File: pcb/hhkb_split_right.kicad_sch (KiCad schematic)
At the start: 73 parts, among them SW1 keyswitch, SW10 keyswitch, SW11 keyswitch, SW12 keyswitch, SW13 keyswitch, SW14 keyswitch, SW15 keyswitch, SW16 keyswitch, SW17 keyswitch, SW18 keyswitch, SW19 keyswitch, SW2 keyswitch, SW20 keyswitch, SW21 keyswitch, SW22 keyswitch, SW23 keyswitch, SW24 keyswitch, SW25 keyswitch, SW26 keyswitch, SW27 keyswitch, SW28 keyswitch, SW29 keyswitch, SW3 keyswitch, SW30 keyswitch, SW31 keyswitch, SW32 keyswitch, SW33 keyswitch, SW34 keyswitch, SW4 keyswitch, SW5 keyswitch, SW6 keyswitch, SW7 keyswitch, SW8 keyswitch, SW9 keyswitch, U1 74LVC595, U2 74LVC595

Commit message: #49 をビア/窓の露出方式で決着——部品も配線も足さず既存の銅のレジストを剥がす
利用者の提案（テストパッドは取り消し済み）。finalize_pcb.expose_debug_copper が
本番の板を作るたびに、ネットごとに他ネットの銅から最も離れた 1 点を選び:
- ビアがあれば裏面（部品面）のテンティングを外す（右: SPI_SCK/SPI_MOSI/CS/
  U1_U2/V3V3 + GND）
- ビアが無ければ配線に沿った B.Mask の窓 2.5×0.5 を開ける（左: SPI 系 4 本。
  左の SPI は全部 B.Cu だけで引かれていてビアが無い）+ GND ビア
窓幅 0.8 は隣の銅とのレジスト残りが規定を割り DRC 8 件 → 0.5 で解消。
定数は pcb_rules.py（検査環境に pcbnew が無いため）。
検査 test_every_debug_net_has_exposed_copper を追加（故意に戻して赤を確認）。
3 基板とも DRC 0/0。半田付けは AWG30 級・細いこて前提（open-gaps #49 に注記）。

Co-Authored-By: Claude Fable 5 <noreply@anthropic.com>
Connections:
- net COL0: now also SW18.1, SW25.1, SW32.1
- net COL1: now also SW17.1, SW31.1; no longer SW18.1, SW25.1, SW32.1
- net COL8: no longer SW17.1, SW31.1
- net CS: now also J_DB.4; no longer J_DB.1
- net GND: now also J_DB.1; no longer J_DB.12, J_DB.5
- net SPI_MOSI: now also J_DB.3; no longer J_DB.4
- net SPI_SCK: now also J_DB.5; no longer J_DB.3
- net SPARE2: now reaches J_DB.6
- net ROW0 renamed ROW_C
- net ROW_C: now also J_DB.10; no longer J_DB.7
- net ROW1 renamed ROW_A
- net ROW2 renamed ROW_B
- net ROW_B: now also J_DB.9; no longer J_DB.11
- net ROW3 renamed ROW_D
- net ROW_D: now also J_DB.11; no longer J_DB.10
- net ROW4 renamed ROW_E
- net ROW_E: now also J_DB.12; no longer J_DB.9
- new net SPARE: J_DB.7
- no-connect marks 9 -> 8
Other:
- moved on the sheet: D1, D10, D11, D12, D13, D14, D15, D16, D17, D18, D19, D2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

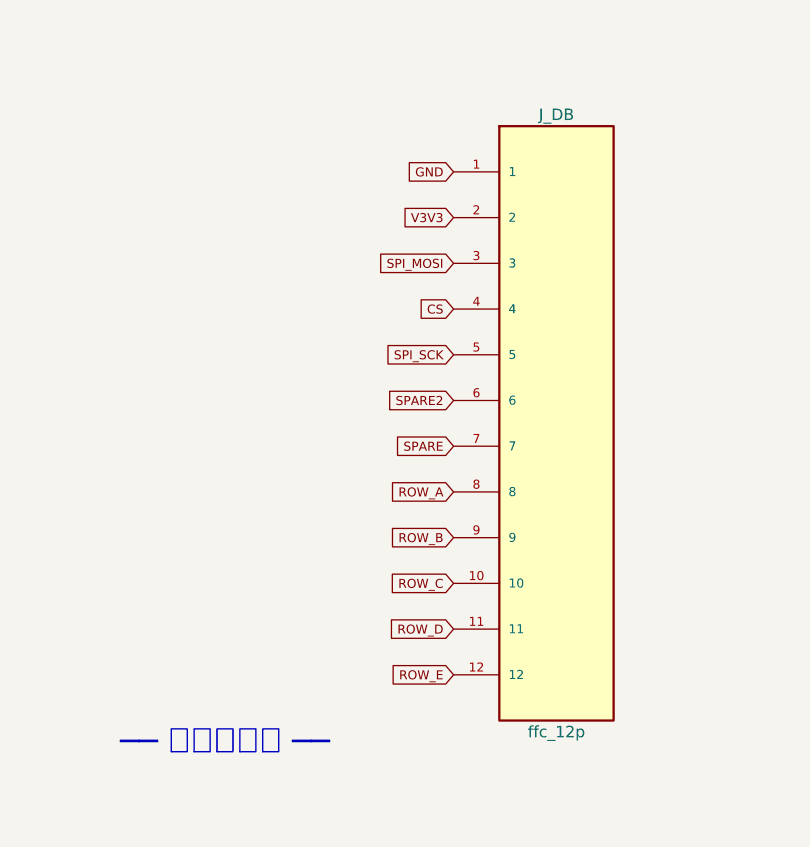
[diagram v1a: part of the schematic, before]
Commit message: #19 J_DB の口を奥向きに回した（FFC は直線・A タイプで正しい）。左は配線無傷で DRC 0、右は J_DB 周りの引き直し待ち
- 原因: 2026-08-08 の初回配置で Flip() の副作用の 180° をそのまま使い、誰も口の向きを決めていなかった（git 履歴で確認）
- circuit.py: J_DB のピン表を J_MAIN の鏡像（n ↔ 13-n）に。裏面で 180° 回すとピン 1 の側が入れ替わるため。検査 2 本と決定文書を鏡像に更新
- gen_pcb.py: J_DB に向き 0° と dy（左 -3.7 / 右 -0.4）。配置は matrix_only の現物が優先
- 左 matrix_only: J_DB を 0°・3.7mm 奥へ → 12 パッドが同じ座標に戻り配線無傷。DRC 0/0
- 右 matrix_only: 3.7mm は SW10 の NPTH がコートヤードに入るため 0.4mm 止まり。パッドが南側の枝と重なり DRC 違反 20・未配線 8（利用者の引き直し・open-gaps #19 に手順）
- gen_assembly.py: 幕と床走行を消し、口の直後の潜り＋J_MAIN までの斜めのリボンに。箱モード干渉 0
- 回路図・部品記録・DRC 記録・証拠ページを更新。検査 455 緑・5 赤（全部右の引き直しと露出ビアの打ち直しに帰着・open-gaps に列挙）

Co-Authored-By: Claude Fable 5 <noreply@anthropic.com>
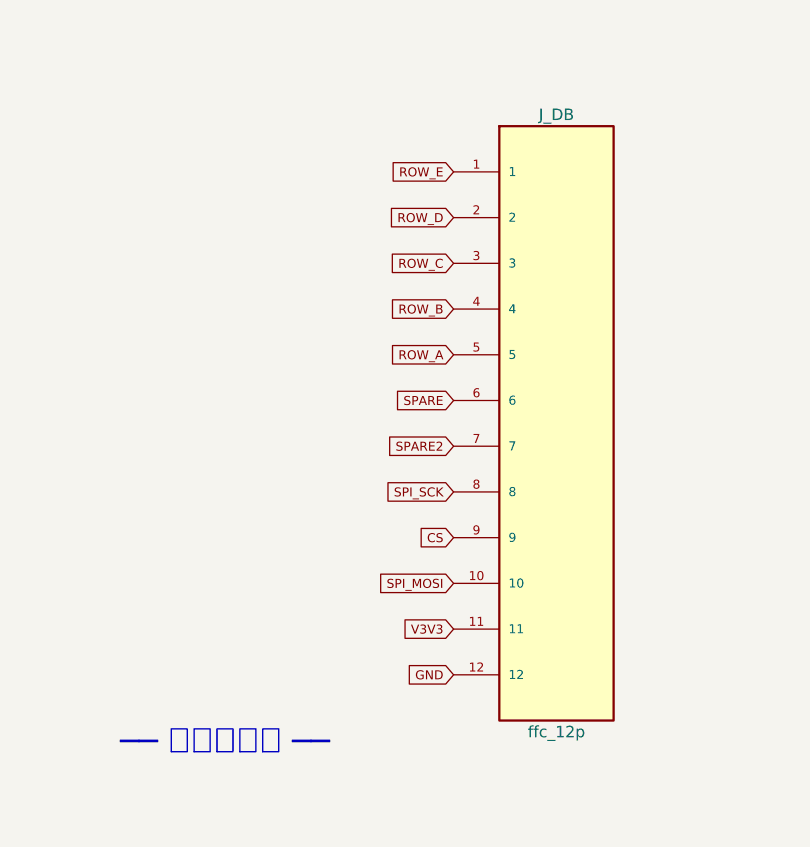
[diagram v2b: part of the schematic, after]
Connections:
- net CS: now also J_DB.9; no longer J_DB.4
- net GND: now also J_DB.11, J_DB.12; no longer J_DB.1, J_DB.2
- net ROW_A: now also J_DB.5; no longer J_DB.8
- net ROW_B: now also J_DB.4; no longer J_DB.9
- net ROW_C: now also J_DB.3; no longer J_DB.10
- net ROW_D: now also J_DB.2; no longer J_DB.11
- net ROW_E: now also J_DB.1; no longer J_DB.12
- net SPARE: now also J_DB.6; no longer J_DB.7
- net SPARE2: now also J_DB.7; no longer J_DB.6
- net SPI_MOSI: now also J_DB.10; no longer J_DB.3
- net SPI_SCK: now also J_DB.8; no longer J_DB.5
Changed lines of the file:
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@@
 	)
 	(global_label
-		"GND"
+		"ROW_E"
 		(shape input)
 		(at 63.50 248.92 180)
@@
 	)
 	(global_label
-		"V3V3"
+		"ROW_D"
 		(shape input)
 		(at 63.50 254.00 180)
@@
 	)
 	(global_label
-		"SPI_MOSI"
+		"ROW_C"
 		(shape input)
 		(at 63.50 259.08 180)
@@
 	)
 	(global_label
-		"CS"
+		"ROW_B"
 		(shape input)
 		(at 63.50 264.16 180)
@@
 	)
 	(global_label
-		"SPI_SCK"
+		"ROW_A"
 		(shape input)
 		(at 63.50 269.24 180)
@@
 	)
 	(global_label
-		"SPARE2"
+		"SPARE"
 		(shape input)
 		(at 63.50 274.32 180)
@@
 	)
 	(global_label
-		"SPARE"
+		"SPARE2"
 		(shape input)
 		(at 63.50 279.40 180)
@@
 	)
 	(global_label
-		"ROW_A"
+		"SPI_SCK"
 		(shape input)
 		(at 63.50 284.48 180)
@@
 	)
 	(global_label
-		"ROW_B"
+		"CS"
 		(shape input)
 		(at 63.50 289.56 180)
@@
 	)
 	(global_label
-		"ROW_C"
+		"SPI_MOSI"
 		(shape input)
 		(at 63.50 294.64 180)
@@
 	)
 	(global_label
-		"ROW_D"
+		"V3V3"
 		(shape input)
 		(at 63.50 299.72 180)
@@
 	)
 	(global_label
-		"ROW_E"
+		"GND"
 		(shape input)
 		(at 63.50 304.80 180)
